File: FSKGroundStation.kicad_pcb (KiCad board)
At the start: 4 copper layers, 100 x 82 mm, 206 parts, among them J1 FTSH-105-01-L-DV-K, J10 CX90B1-24P, J11 HTSW-102-07-G-S, J22 BWSMA-KWE-Z001, J23 SJ-3524-SMT, J24 HTSW-103-07-G-S, J25 PJ-063BH, J3 CX90B1-24P, J4 BWSMA-KWE-Z001, J5 BWSMA-KWE-Z001, J9 HTSW-102-07-G-S, Q1 BSS138, Q2 BSS138, U1 TPSM861253RDXR, U10 74LVC1GU04DRL, U2 CC1312R1F3RGZR, U3 CY7C65215-32LTXI, U4 CC1125RHBR, U5 GRF5604, U6 SKYA21003, U7 GRF5604, U8 TPD4E004DRYR, U9 SKYA21003, Y1 OW7EL89CENUYO3YLC-40M, Y2 OW7EL89CANUXK7YLC-48M

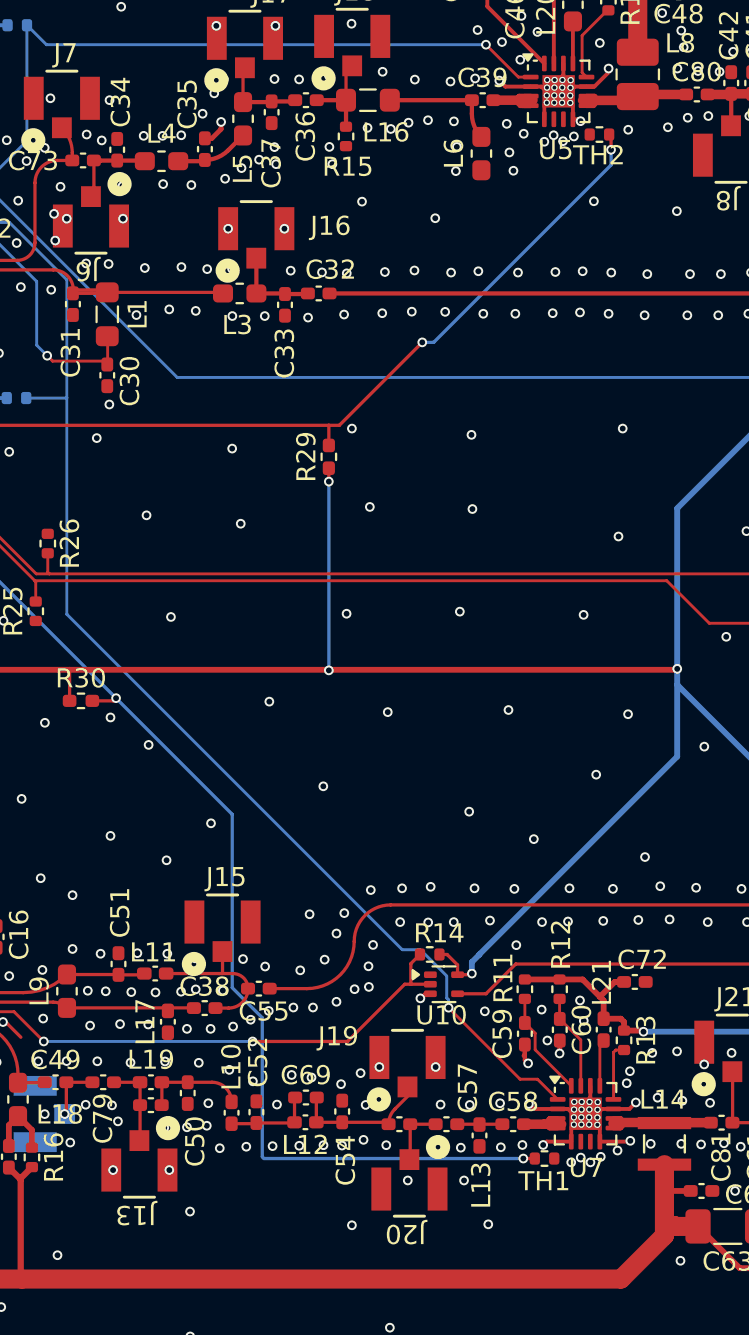
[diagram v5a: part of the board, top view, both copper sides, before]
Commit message: Adjust the thermsistors a bit
Keep the bottom ground plan as clean as possible, make sure there are
plenty of vias around the termsistor, and avoid messing up the coplanar
areas around some RF traces.

Signed-off-by: Corey Minyard <corey@minyard.net>
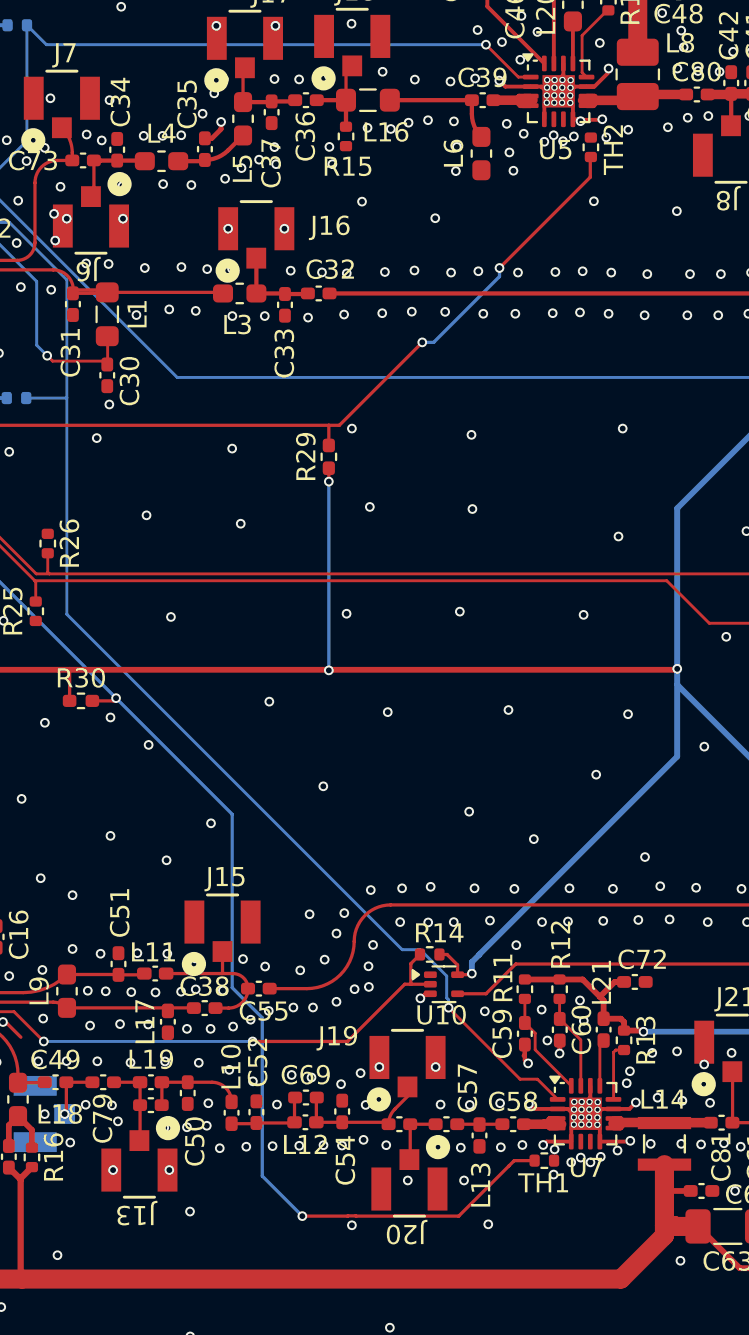
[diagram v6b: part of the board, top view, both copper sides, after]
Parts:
- R27, R28, R97: value 10KΩ -> 10K
- R29, R30: value 10KΩ 1% -> 10K 1%
- moved TH2 0.81 mm to (137.0, 76.2), turned to 90 degrees
- moved TH1 0.11 mm to (134.6, 129.3)
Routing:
- net 440_PA_TEMP: track 69.9 -> 72.9 mm
- net 144_PA_TEMP: track 52.6 -> 51.1 mm
- net GND: track 103.9 -> 104.9 mm, vias 609 -> 613
